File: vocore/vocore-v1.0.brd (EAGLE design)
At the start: 25.6 x 25.6 mm, 146 parts, among them CON2 5020, U1 TFBGA196, U25 U4, U3 SO8, U33 Y1, U35 TSOP2-54P-400MIL, U8 LDO1, U9 LDO1

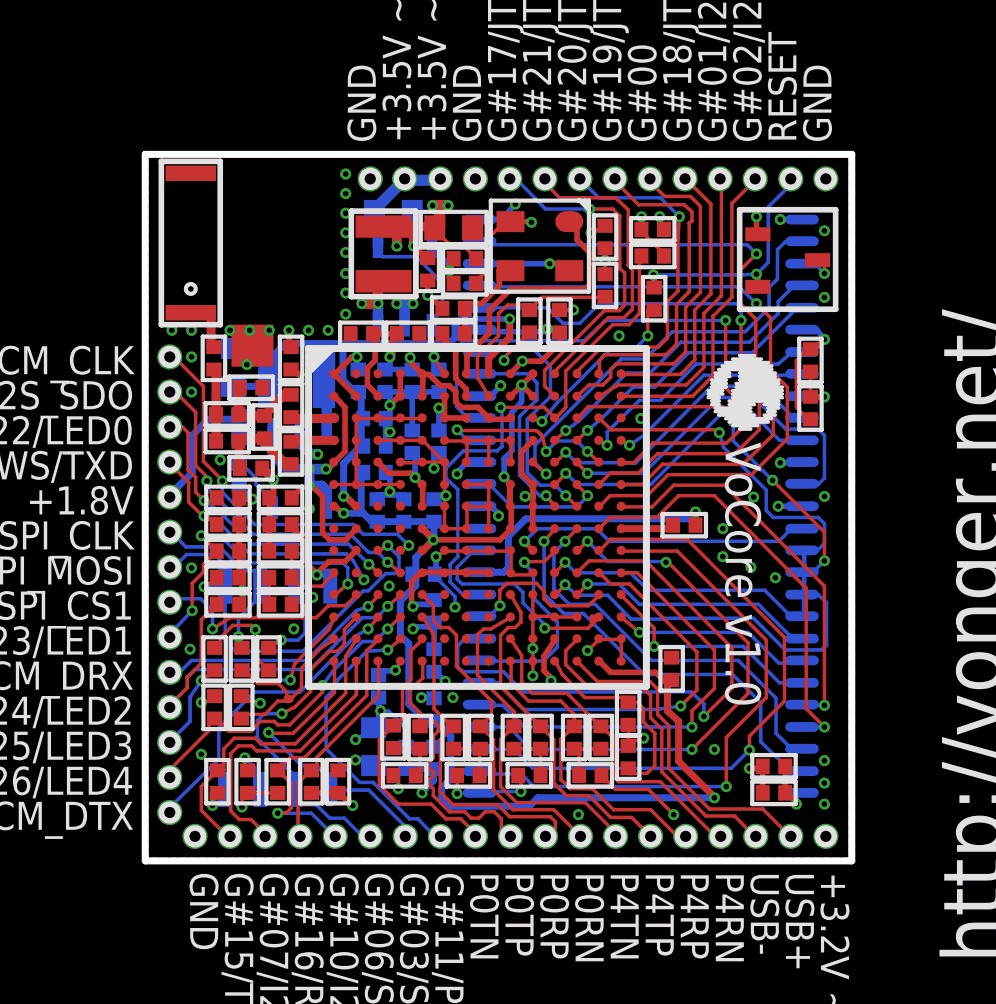
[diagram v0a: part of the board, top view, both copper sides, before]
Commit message: removed a bad trace when i was fixing short airwires.
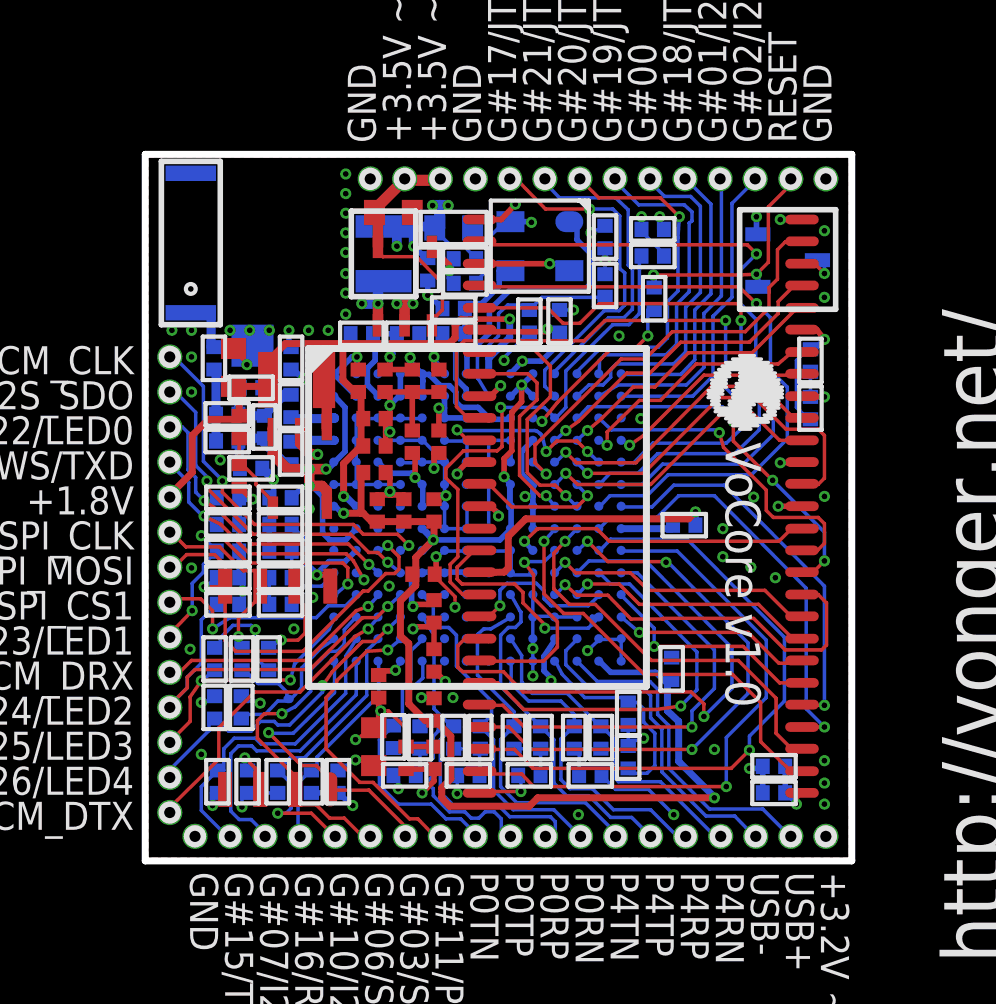
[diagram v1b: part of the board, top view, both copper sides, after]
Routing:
- net SDRAM_CS: track 12.2 -> 10.0 mm
